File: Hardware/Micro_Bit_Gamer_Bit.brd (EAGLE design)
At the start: 152.4 x 50.8 mm, 37 parts, among them J1 Pokehome, J2 Pokehome, J3 Pokehome, J4 Pokehome, J5 Pokehome, J6 Pokehome, J7 Pokehome, J8 Pokehome, U1 micro:bit

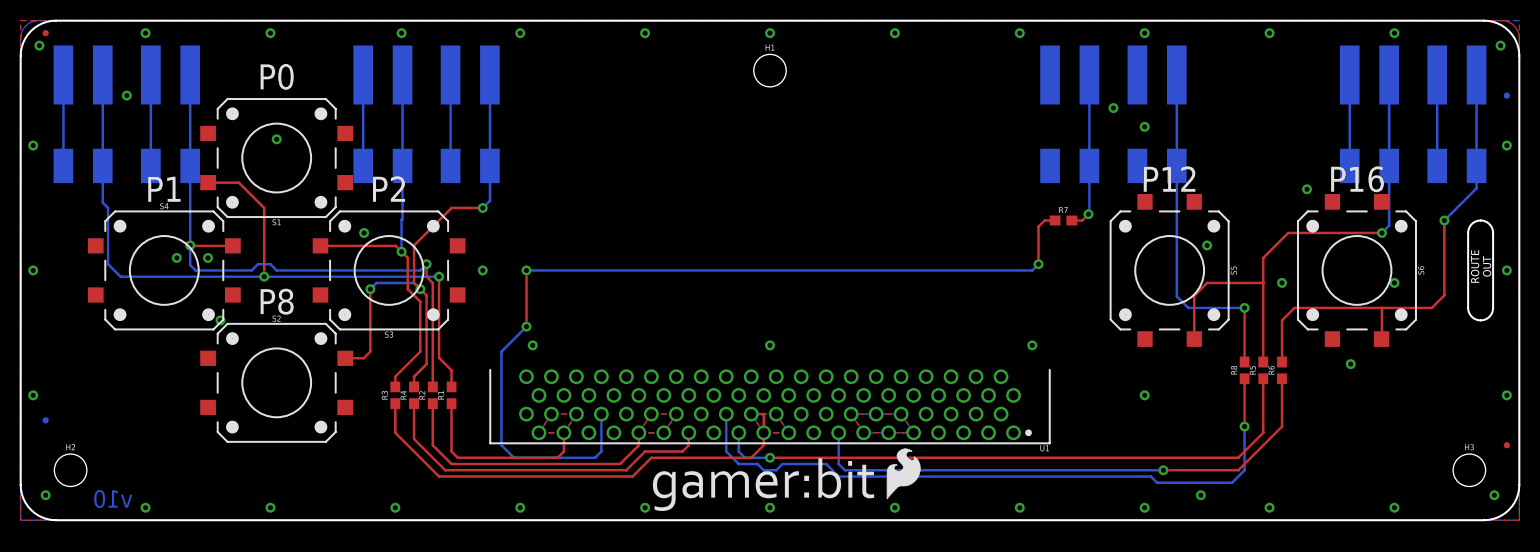
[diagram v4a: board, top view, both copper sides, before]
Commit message: Moved to SMD connector
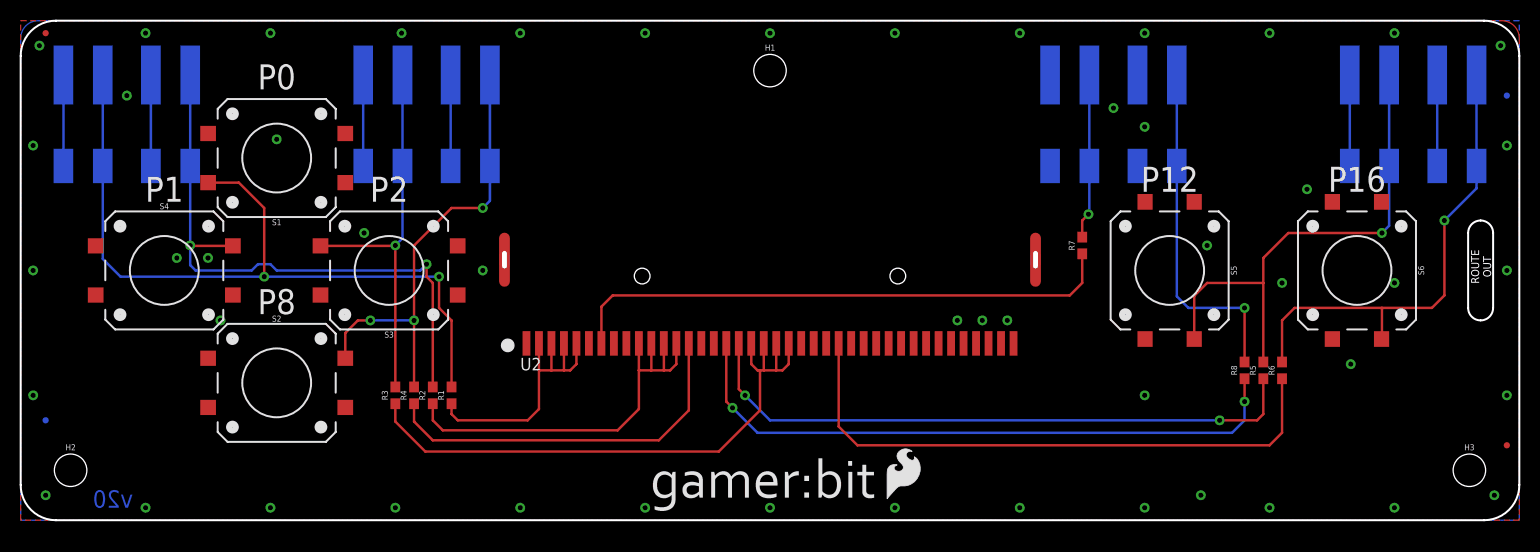
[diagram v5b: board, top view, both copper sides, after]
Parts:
- removed U1: micro:bit, Micro_Bit_Parts:MICRO:BIT_RA_PTH
- added U2: micro:bit, SparkFun-Connectors:MICRO:BIT-RA_SMD
- moved R7 3.18 mm to (108.0, 27.9), turned to 90 degrees
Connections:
- net 3.3V: now also U2.P$27, U2.P$28, U2.P$29, U2.P$30, U2.P$31, U2.P$32; no longer U1.A10, U1.A11, U1.A12, U1.A13, U1.A14, U1.A9
- net BTN_A: now also U2.P$7; no longer U1.A34
- net BTN_B: now also U2.P$17; no longer U1.A24
- net BTN_DN: now also U2.P$14; no longer U1.A27
- net BTN_L: now also U2.P$10, U2.P$11, U2.P$12, U2.P$13; no longer U1.A28, U1.A29, U1.A30, U1.A31
- net BTN_P12: now also U2.P$18; no longer U1.A23
- net BTN_P16: now also U2.P$26; no longer U1.A15
- net BTN_R: now also U2.P$19, U2.P$20, U2.P$21, U2.P$22; no longer U1.A19, U1.A20, U1.A21, U1.A22
- net BTN_UP: now also U2.P$2, U2.P$3, U2.P$4, U2.P$5; no longer U1.A36, U1.A37, U1.A38, U1.A39
- net GND: now also U2.P$35, U2.P$36, U2.P$37, U2.P$38, U2.P$39, U2.P$40; no longer U1.A1, U1.A2, U1.A3, U1.A4, U1.A5, U1.A6
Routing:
- net BTN_A: track 91.7 -> 56.6 mm, vias 3 -> 0
- net BTN_L: track 28.0 -> 42.3 mm
- net BTN_R: track 48.0 -> 60.0 mm
- net BTN_UP: track 18.7 -> 29.0 mm
- net N$3: track 52.6 -> 46.9 mm
- net BTN_P16: track 55.2 -> 60.4 mm, vias 1 -> 0
- net BTN_B: track 68.2 -> 64.7 mm, vias 1 -> 2
- net BTN_DN: track 35.2 -> 38.6 mm
- net N$4: track 42.2 -> 39.7 mm
- net BTN_P12: track 62.1 -> 63.2 mm, vias 1 -> 2
- net N$7: track 16.2 -> 16.8 mm
- removed copper zone on layer 1, net 3.3V
- removed copper zone on layer 16, net 3.3V
- removed copper zone on layer 1, net BTN_L
- removed copper zone on layer 16, net BTN_L
- removed copper zone on layer 1, net BTN_R
- removed copper zone on layer 16, net BTN_R
- removed copper zone on layer 1, net BTN_UP
- removed copper zone on layer 16, net BTN_UP
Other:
- board text added: "Revised by: Pete Lewis"
- board text added: "v20"
- board text removed: "v10"

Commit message: Update silk to control bit
On both front and back.
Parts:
- removed U$2, U$3: LOGO-GAMERBIT, Micro_Bit_Parts:LOGO-GAMERBIT
- added U$4, U$5: LOGO-CONTROLBIT, Micro_Bit_Parts:LOGO-CONTROLBIT
- moved LOGO1 3.44 mm to (91.2, 2.48)
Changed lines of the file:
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@@
 <setting verticaltext="up"/>
 </settings>
-<grid distance="0.05" unitdist="inch" unit="inch" style="lines" multiple="1" display="yes" altdistance="0.005" altunitdist="inch" altunit="inch"/>
+<grid distance="0.00125" unitdist="inch" unit="inch" style="lines" multiple="1" display="yes" altdistance="0.005" altunitdist="inch" altunit="inch"/>
 <layers>
 <layer number="1" name="Top" color="4" fill="1" visible="yes" active="yes"/>
@@
 <layer number="17" name="Pads" color="2" fill="1" visible="yes" active="yes"/>
 <layer number="18" name="Vias" color="2" fill="1" visible="yes" active="yes"/>
-<layer number="19" name="Unrouted" color="6" fill="1" visible="yes" active="yes"/>
-<layer number="20" name="Dimension" color="15" fill="1" visible="yes" active="yes"/>
+<layer number="19" name="Unrouted" color="6" fill="1" visible="no" active="yes"/>
+<layer number="20" name="Dimension" color="15" fill="1" visible="no" active="yes"/>
 <layer number="21" name="tPlace" color="16" fill="1" visible="yes" active="yes"/>
 <layer number="22" name="bPlace" color="14" fill="1" visible="yes" active="yes"/>
@@
 <layer number="27" name="tValues" color="7" fill="1" visible="no" active="yes"/>
 <layer number="28" name="bValues" color="7" fill="1" visible="no" active="yes"/>
-<layer number="29" name="tStop" color="7" fill="3" visible="no" active="yes"/>
+<layer number="29" name="tStop" color="7" fill="3" visible="yes" active="yes"/>
 <layer number="30" name="bStop" color="7" fill="6" visible="no" active="yes"/>
 <layer number="31" name="tCream" color="7" fill="4" visible="no" active="yes"/>
@@
 <layer number="43" name="vRestrict" color="2" fill="10" visible="no" active="yes"/>
 <layer number="44" name="Drills" color="7" fill="1" visible="no" active="yes"/>
-<layer number="45" name="Holes" color="7" fill="1" visible="yes" active="yes"/>
+<layer number="45" name="Holes" color="7" fill="1" visible="no" active="yes"/>
 <layer number="46" name="Milling" color="3" fill="1" visible="no" active="yes"/>
 <layer number="47" name="Measures" color="7" fill="1" visible="no" active="yes"/>
 <layer number="48" name="Document" color="7" fill="1" visible="no" active="yes"/>
-<layer number="49" name="Reference" color="7" fill="1" visible="yes" active="yes"/>
+<layer number="49" name="Reference" color="7" fill="1" visible="no" active="yes"/>
 <layer number="50" name="dxf" color="7" fill="1" visible="no" active="no"/>
-<layer number="51" name="tDocu" color="6" fill="1" visible="yes" active="yes"/>
+<layer number="51" name="tDocu" color="6" fill="1" visible="no" active="yes"/>
 <layer number="52" name="bDocu" color="7" fill="1" visible="no" active="yes"/>
 <layer number="53" name="tGND_GNDA" color="7" fill="9" visible="no" active="no"/>
@@
 <layer number="155" name="FabDoc3" color="7" fill="1" visible="no" active="yes"/>
 <layer number="199" name="Contour" color="7" fill="1" visible="no" active="yes"/>
-<layer number="200" name="200bmp" color="1" fill="10" visible="no" active="yes"/>
+<layer number="200" name="200bmp" color="1" fill="10" visible="yes" active="yes"/>
 <layer number="201" name="201bmp" color="2" fill="10" visible="no" active="yes"/>
 <layer number="202" name="202bmp" color="3" fill="10" visible="no" active="yes"/>
@@
 <attribute name="PROD_ID" value="CONN-13512" x="146.05" y="41.275" size="1.778" layer="28" font="vector" ratio="15" rot="MR270" display="off"/>
 </element>
-<element name="LOGO1" library="SparkFun-Aesthetics" package="SFE_LOGO_FLAME_.2" value="SFE_LOGO_FLAME.2_INCH" x="87.757" y="1.905" smashed="yes"/>
+<element name="LOGO1" library="SparkFun-Aesthetics" package="SFE_LOGO_FLAME_.2" value="SFE_LOGO_FLAME.2_INCH" x="91.15425" y="2.4765" smashed="yes"/>
 <element name="LOGO2" library="SparkFun-Aesthetics" package="OSHW-LOGO-L" value="OSHW-LOGOL" x="76.2" y="25.4" smashed="yes" rot="MR0"/>
 <element name="LOGO3" library="SparkFun-Aesthetics" package="SFE_LOGO_NAME_FLAME_.3" value="SFE_LOGO_NAME_FLAME.3_INCH" x="92.71" y="34.29" smashed="yes" rot="MR0"/>
@@
 <element name="FD3" library="SparkFun-Aesthetics" package="FIDUCIAL-MICRO" value="FIDUCIALUFIDUCIAL" x="2.54" y="10.16" smashed="yes" rot="MR0"/>
 <element name="FD4" library="SparkFun-Aesthetics" package="FIDUCIAL-MICRO" value="FIDUCIALUFIDUCIAL" x="151.13" y="43.18" smashed="yes" rot="MR0"/>
-<element name="U$2" library="Micro_Bit_Parts" package="LOGO-GAMERBIT" value="LOGO-GAMERBIT" x="64.135" y="0.762" smashed="yes"/>
-<element name="U$3" library="Micro_Bit_Parts" package="LOGO-GAMERBIT" value="LOGO-GAMERBIT" x="87.63" y="29.083" smashed="yes" rot="MR0"/>
 <element name="U2" library="SparkFun-Connectors" package="MICRO:BIT-RA_SMD" value="micro:bit" x="76.2" y="24.13" smashed="yes">
 <attribute name="NAME" x="50.8" y="15.24" size="1.27" layer="25" font="vector"/>
@@
 <attribute name="VALUE" x="95.25" y="15.24" size="1.27" layer="27" font="vector"/>
 </element>
+<element name="U$4" library="Micro_Bit_Parts" package="LOGO-CONTROLBIT" value="LOGO-CONTROLBIT" x="58.95975" y="2.8575" smashed="yes"/>
+<element name="U$5" library="Micro_Bit_Parts" package="LOGO-CONTROLBIT" value="LOGO-CONTROLBIT" x="91.97975" y="30.4165" smashed="yes" rot="MR0"/>
 </elements>
 <signals>

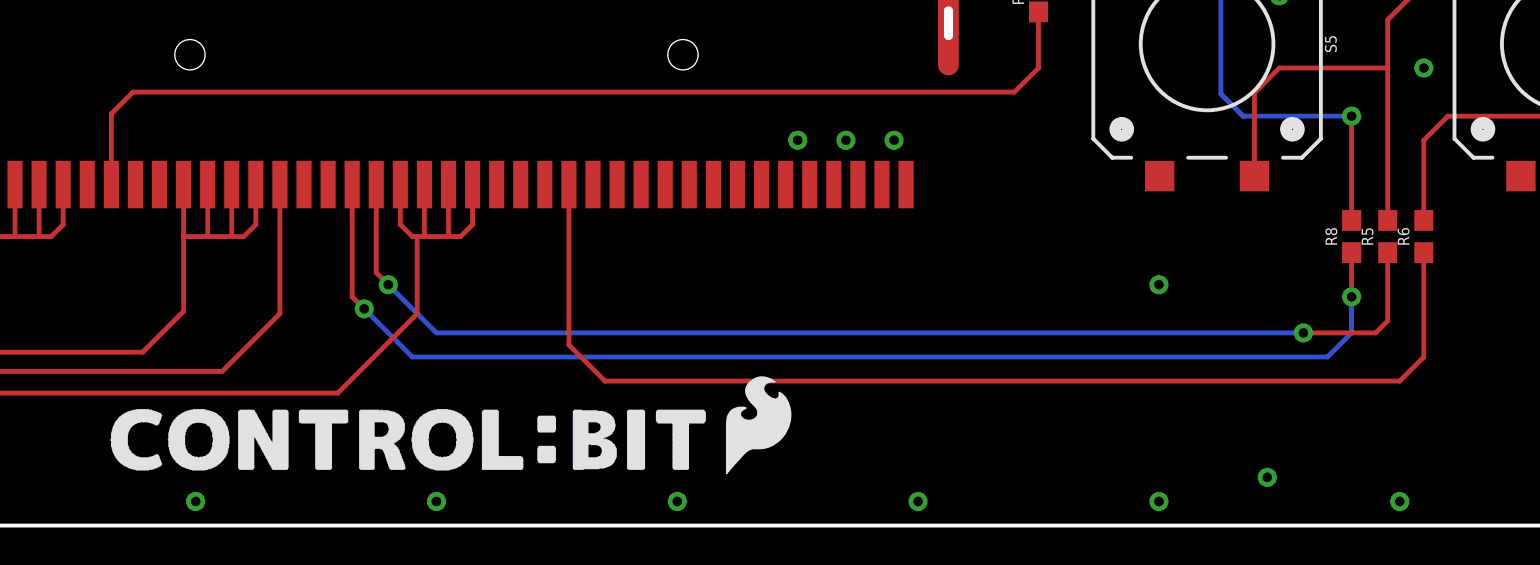
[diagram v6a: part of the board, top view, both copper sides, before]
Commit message: Cleaned up a coulpe traces added vias for pour
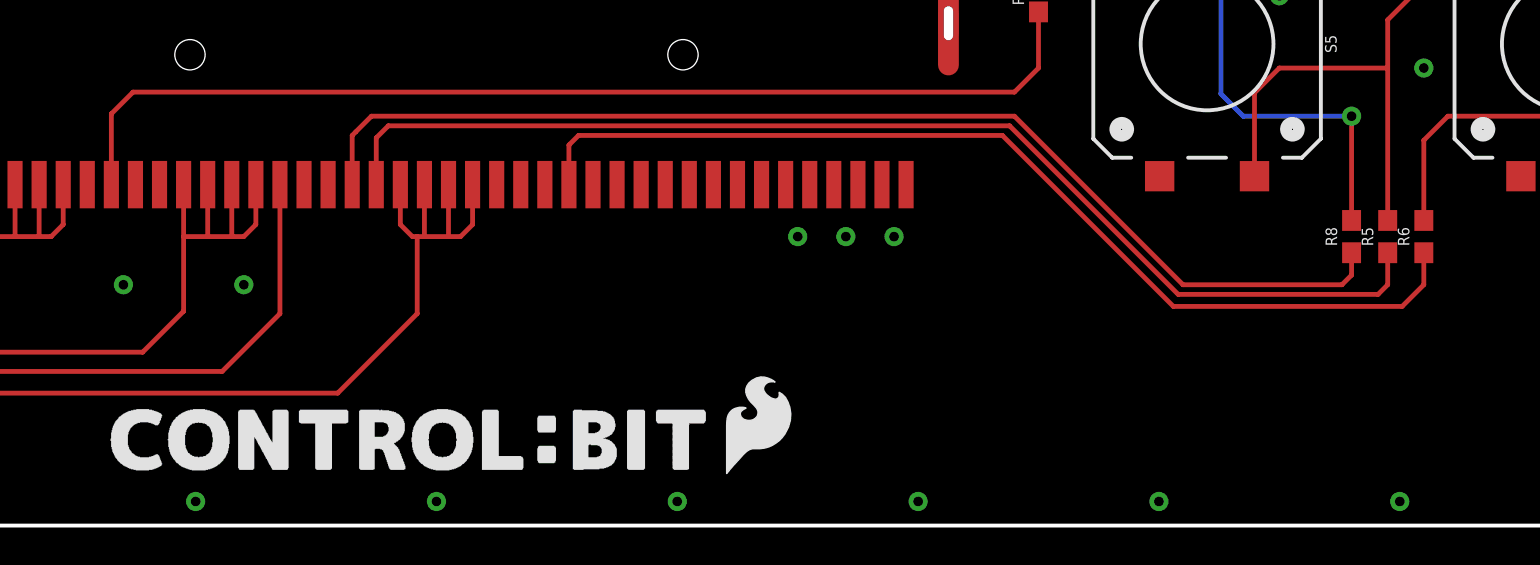
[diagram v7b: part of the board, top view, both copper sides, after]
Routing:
- net BTN_P16: track 60.4 -> 53.3 mm
- net BTN_B: track 64.7 -> 60.8 mm, vias 2 -> 0
- net BTN_P12: track 63.2 -> 61.7 mm, vias 2 -> 0
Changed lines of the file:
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@@
 <setting verticaltext="up"/>
 </settings>
-<grid distance="0.00125" unitdist="inch" unit="inch" style="lines" multiple="1" display="yes" altdistance="0.005" altunitdist="inch" altunit="inch"/>
+<grid distance="0.05" unitdist="inch" unit="inch" style="lines" multiple="1" display="yes" altdistance="0.005" altunitdist="inch" altunit="inch"/>
 <layers>
 <layer number="1" name="Top" color="4" fill="1" visible="yes" active="yes"/>
@@
 <layer number="17" name="Pads" color="2" fill="1" visible="yes" active="yes"/>
 <layer number="18" name="Vias" color="2" fill="1" visible="yes" active="yes"/>
-<layer number="19" name="Unrouted" color="6" fill="1" visible="no" active="yes"/>
-<layer number="20" name="Dimension" color="15" fill="1" visible="no" active="yes"/>
+<layer number="19" name="Unrouted" color="6" fill="1" visible="yes" active="yes"/>
+<layer number="20" name="Dimension" color="15" fill="1" visible="yes" active="yes"/>
 <layer number="21" name="tPlace" color="16" fill="1" visible="yes" active="yes"/>
 <layer number="22" name="bPlace" color="14" fill="1" visible="yes" active="yes"/>
@@
 <layer number="27" name="tValues" color="7" fill="1" visible="no" active="yes"/>
 <layer number="28" name="bValues" color="7" fill="1" visible="no" active="yes"/>
-<layer number="29" name="tStop" color="7" fill="3" visible="yes" active="yes"/>
+<layer number="29" name="tStop" color="7" fill="3" visible="no" active="yes"/>
 <layer number="30" name="bStop" color="7" fill="6" visible="no" active="yes"/>
 <layer number="31" name="tCream" color="7" fill="4" visible="no" active="yes"/>
@@
 <layer number="43" name="vRestrict" color="2" fill="10" visible="no" active="yes"/>
 <layer number="44" name="Drills" color="7" fill="1" visible="no" active="yes"/>
-<layer number="45" name="Holes" color="7" fill="1" visible="no" active="yes"/>
+<layer number="45" name="Holes" color="7" fill="1" visible="yes" active="yes"/>
 <layer number="46" name="Milling" color="3" fill="1" visible="no" active="yes"/>
 <layer number="47" name="Measures" color="7" fill="1" visible="no" active="yes"/>
 <layer number="48" name="Document" color="7" fill="1" visible="no" active="yes"/>
-<layer number="49" name="Reference" color="7" fill="1" visible="no" active="yes"/>
+<layer number="49" name="Reference" color="7" fill="1" visible="yes" active="yes"/>
 <layer number="50" name="dxf" color="7" fill="1" visible="no" active="no"/>
-<layer number="51" name="tDocu" color="6" fill="1" visible="no" active="yes"/>
+<layer number="51" name="tDocu" color="6" fill="1" visible="yes" active="yes"/>
 <layer number="52" name="bDocu" color="7" fill="1" visible="no" active="yes"/>
 <layer number="53" name="tGND_GNDA" color="7" fill="9" visible="no" active="no"/>
@@
 <layer number="155" name="FabDoc3" color="7" fill="1" visible="no" active="yes"/>
 <layer number="199" name="Contour" color="7" fill="1" visible="no" active="yes"/>
-<layer number="200" name="200bmp" color="1" fill="10" visible="yes" active="yes"/>
+<layer number="200" name="200bmp" color="1" fill="10" visible="no" active="yes"/>
 <layer number="201" name="201bmp" color="2" fill="10" visible="no" active="yes"/>
 <layer number="202" name="202bmp" color="3" fill="10" visible="no" active="yes"/>
@@
 <contactref element="R6" pad="1"/>
 <contactref element="U2" pad="P$26"/>
-<wire x1="128.27" y1="14.39" x2="128.27" y2="8.89" width="0.254" layer="1"/>
-<wire x1="128.27" y1="8.89" x2="127" y2="7.62" width="0.254" layer="1"/>
-<wire x1="127" y1="7.62" x2="85.09" y2="7.62" width="0.254" layer="1"/>
-<wire x1="83.185" y1="9.525" x2="83.185" y2="17.98" width="0.254" layer="1"/>
-<wire x1="85.09" y1="7.62" x2="83.185" y2="9.525" width="0.254" layer="1"/>
+<wire x1="128.27" y1="14.39" x2="128.27" y2="12.7" width="0.254" layer="1"/>
+<wire x1="128.27" y1="12.7" x2="127.127" y2="11.557" width="0.254" layer="1"/>
+<wire x1="127.127" y1="11.557" x2="115.062" y2="11.557" width="0.254" layer="1"/>
+<wire x1="115.062" y1="11.557" x2="106.045" y2="20.574" width="0.254" layer="1"/>
+<wire x1="106.045" y1="20.574" x2="83.693" y2="20.574" width="0.254" layer="1"/>
+<wire x1="83.693" y1="20.574" x2="83.185" y2="20.066" width="0.254" layer="1"/>
+<wire x1="83.185" y1="20.066" x2="83.185" y2="17.98" width="0.254" layer="1"/>
 </signal>
 <signal name="BTN_P12">
 <contactref element="R5" pad="1"/>
 <contactref element="U2" pad="P$18"/>
-<wire x1="126.365" y1="14.39" x2="126.365" y2="10.795" width="0.254" layer="1"/>
-<wire x1="126.365" y1="10.795" x2="125.73" y2="10.16" width="0.254" layer="1"/>
-<wire x1="125.73" y1="10.16" x2="121.92" y2="10.16" width="0.254" layer="1"/>
-<via x="121.92" y="10.16" extent="1-16" drill="0.508"/>
-<wire x1="121.92" y1="10.16" x2="76.2" y2="10.16" width="0.254" layer="16"/>
-<wire x1="76.2" y1="10.16" x2="73.66" y2="12.7" width="0.254" layer="16"/>
-<via x="73.66" y="12.7" extent="1-16" drill="0.508"/>
-<wire x1="73.66" y1="12.7" x2="73.025" y2="13.335" width="0.254" layer="1"/>
-<wire x1="73.025" y1="13.335" x2="73.025" y2="17.98" width="0.254" layer="1"/>
+<wire x1="73.025" y1="17.98" x2="73.025" y2="20.447" width="0.254" layer="1"/>
+<wire x1="73.025" y1="20.447" x2="73.66" y2="21.082" width="0.254" layer="1"/>
+<wire x1="73.66" y1="21.082" x2="106.426" y2="21.082" width="0.254" layer="1"/>
+<wire x1="106.426" y1="21.082" x2="115.316" y2="12.192" width="0.254" layer="1"/>
+<wire x1="115.316" y1="12.192" x2="125.857" y2="12.192" width="0.254" layer="1"/>
+<wire x1="125.857" y1="12.192" x2="126.365" y2="12.7" width="0.254" layer="1"/>
+<wire x1="126.365" y1="12.7" x2="126.365" y2="14.39" width="0.254" layer="1"/>
 </signal>
 <signal name="3.3V">
@@
 <via x="151.13" y="25.4" extent="1-16" drill="0.508"/>
 <via x="151.13" y="38.1" extent="1-16" drill="0.508"/>
-<via x="100.33" y="20.32" extent="1-16" drill="0.508"/>
-<via x="97.79" y="20.32" extent="1-16" drill="0.508"/>
+<via x="100.33" y="15.24" extent="1-16" drill="0.508"/>
+<via x="97.79" y="15.24" extent="1-16" drill="0.508"/>
 <via x="26.035" y="38.735" extent="1-16" drill="0.508"/>
 <via x="20.32" y="20.32" extent="1-16" drill="0.508"/>
 <via x="34.925" y="29.21" extent="1-16" drill="0.508"/>
 <via x="46.99" y="25.4" extent="1-16" drill="0.508"/>
-<via x="114.3" y="12.7" extent="1-16" drill="0.508"/>
-<via x="120.015" y="2.54" extent="1-16" drill="0.508"/>
 <via x="135.255" y="15.875" extent="1-16" drill="0.508"/>
 <via x="139.7" y="24.13" extent="1-16" drill="0.508"/>
@@
 <contactref element="U2" pad="P$35"/>
 <contactref element="U2" pad="P$39"/>
-<via x="95.25" y="20.32" extent="1-16" drill="0.508"/>
+<via x="95.25" y="15.24" extent="1-16" drill="0.508"/>
+<via x="59.69" y="12.7" extent="1-16" drill="0.508"/>
+<via x="66.04" y="12.7" extent="1-16" drill="0.508"/>
 </signal>
 <signal name="N$1">
@@
 <signal name="BTN_B">
 <contactref element="R8" pad="1"/>
-<via x="124.46" y="12.065" extent="1-16" drill="0.508"/>
-<wire x1="124.46" y1="10.16" x2="124.46" y2="12.065" width="0.254" layer="16"/>
-<wire x1="124.46" y1="10.16" x2="123.19" y2="8.89" width="0.254" layer="16"/>
-<wire x1="124.46" y1="14.39" x2="124.46" y2="12.065" width="0.254" layer="1"/>
 <contactref element="U2" pad="P$17"/>
-<wire x1="71.755" y1="17.98" x2="71.755" y2="12.065" width="0.254" layer="1"/>
-<wire x1="71.755" y1="12.065" x2="72.39" y2="11.43" width="0.254" layer="1"/>
-<via x="72.39" y="11.43" extent="1-16" drill="0.508"/>
-<wire x1="72.39" y1="11.43" x2="74.93" y2="8.89" width="0.254" layer="16"/>
-<wire x1="74.93" y1="8.89" x2="123.19" y2="8.89" width="0.254" layer="16"/>
+<wire x1="124.46" y1="14.39" x2="124.46" y2="13.208" width="0.254" layer="1"/>
+<wire x1="124.46" y1="13.208" x2="123.952" y2="12.7" width="0.254" layer="1"/>
+<wire x1="123.952" y1="12.7" x2="115.57" y2="12.7" width="0.254" layer="1"/>
+<wire x1="115.57" y1="12.7" x2="106.68" y2="21.59" width="0.254" layer="1"/>
+<wire x1="106.68" y1="21.59" x2="72.771" y2="21.59" width="0.254" layer="1"/>
+<wire x1="72.771" y1="21.59" x2="71.9455" y2="20.7645" width="0.254" layer="1"/>
+<wire x1="71.755" y1="17.98" x2="71.755" y2="20.574" width="0.254" layer="1"/>
+<wire x1="71.755" y1="20.574" x2="71.9455" y2="20.7645" width="0.254" layer="1"/>
 </signal>
 <signal name="N$7">
